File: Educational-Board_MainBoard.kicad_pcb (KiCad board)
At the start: 2 copper layers, 200 x 75.1 mm, 173 parts, among them J201 Screw_Terminal_01x02_P5mm, J202 USB-C_304A-ACP16X, J401 ACC_INT1, J402 BME_SPI, J403 LUX_INT, J501 RGB_OUT, J601 PWR_IN1, J602 PWR_IN2, J603 PWR_IN3, J604 PWR_IN4, J605 MCP_INT, J606 5V, J607 GND, J608 3V3, J609 EX_PA, J610 EX_PB, J611 PWR_OUT1, J612 PWR_OUT3, J613 PWR_OUT2, J614 PWR_OUT4, Q501 AO3400A, Q601 IRLML9301TRPBF, Q602 IRLML9301TRPBF, Q603 IRLML9301TRPBF, Q604 IRLML9301TRPBF, SW301 RESET, SW501 BUTTON1, SW502 BUTTON2, SW503 BUTTON3, SW504 BUTTON4, SW505 BUTTON5, U201 TPS5430DDA, U202 NUCLEO64-H503RB, U401 LSM6DS3, U402 BME280, U403 OPT4001, U404 INA2180A2, U406 YK16S-L7.2-B10Ka(32-8)-G-A29, U501 74LVC1G34, U502 SSD1315 OLED 0.98", U603 MCP23017_SS

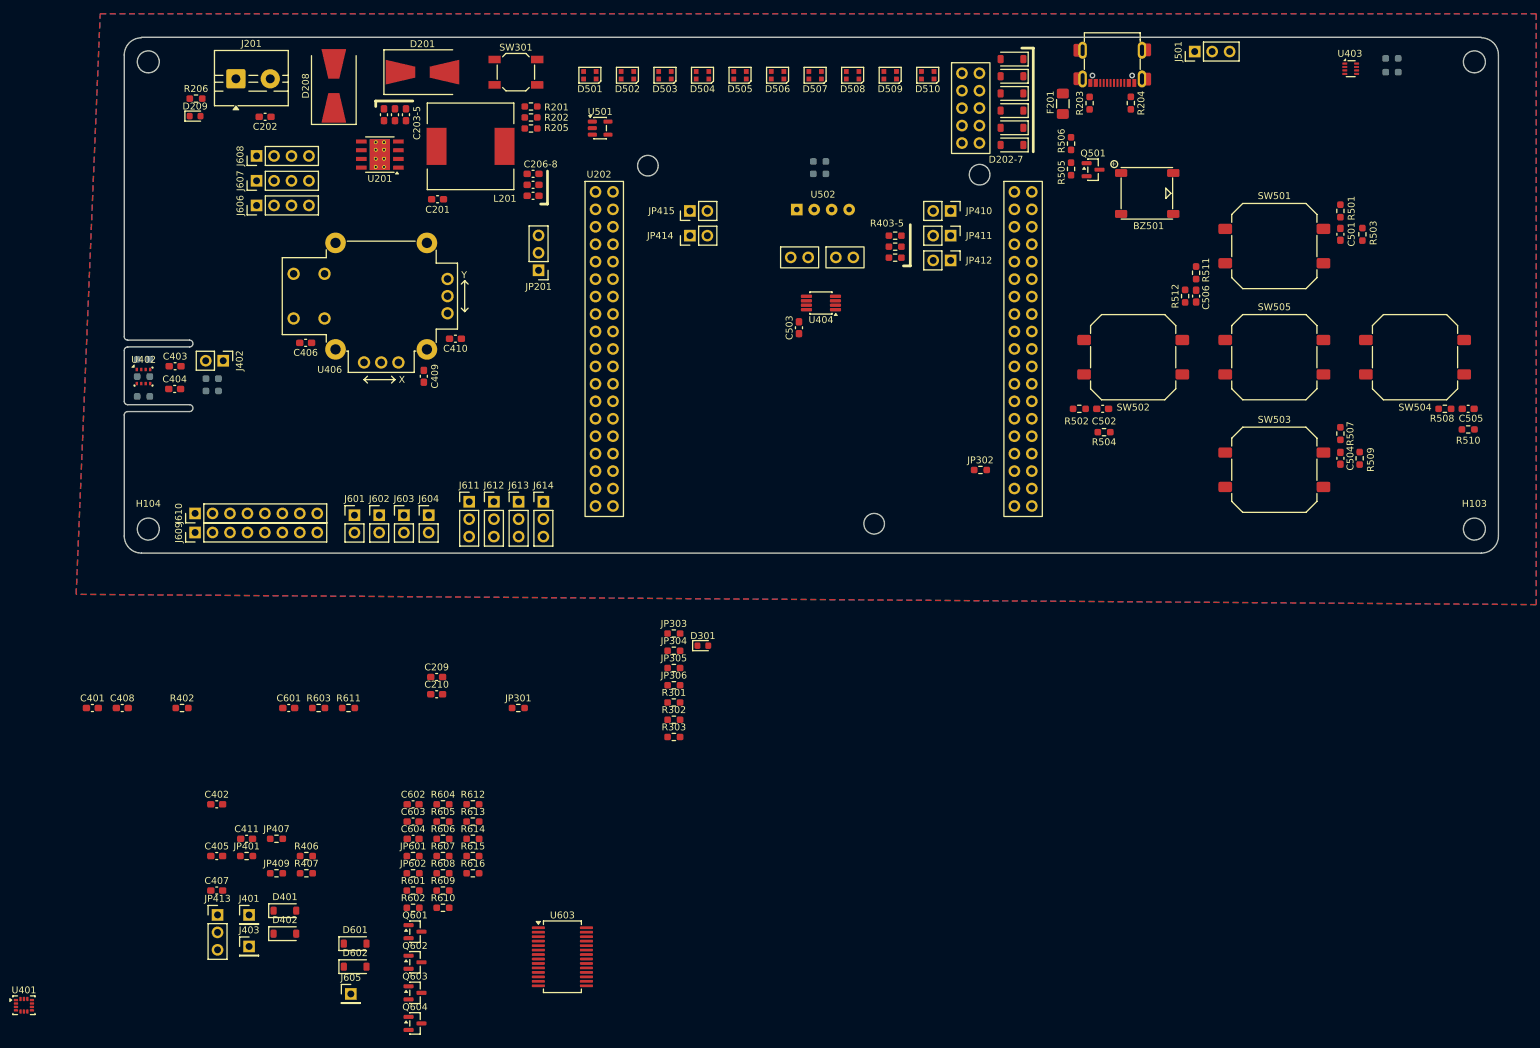
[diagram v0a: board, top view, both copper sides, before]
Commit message: Continued the floor plan
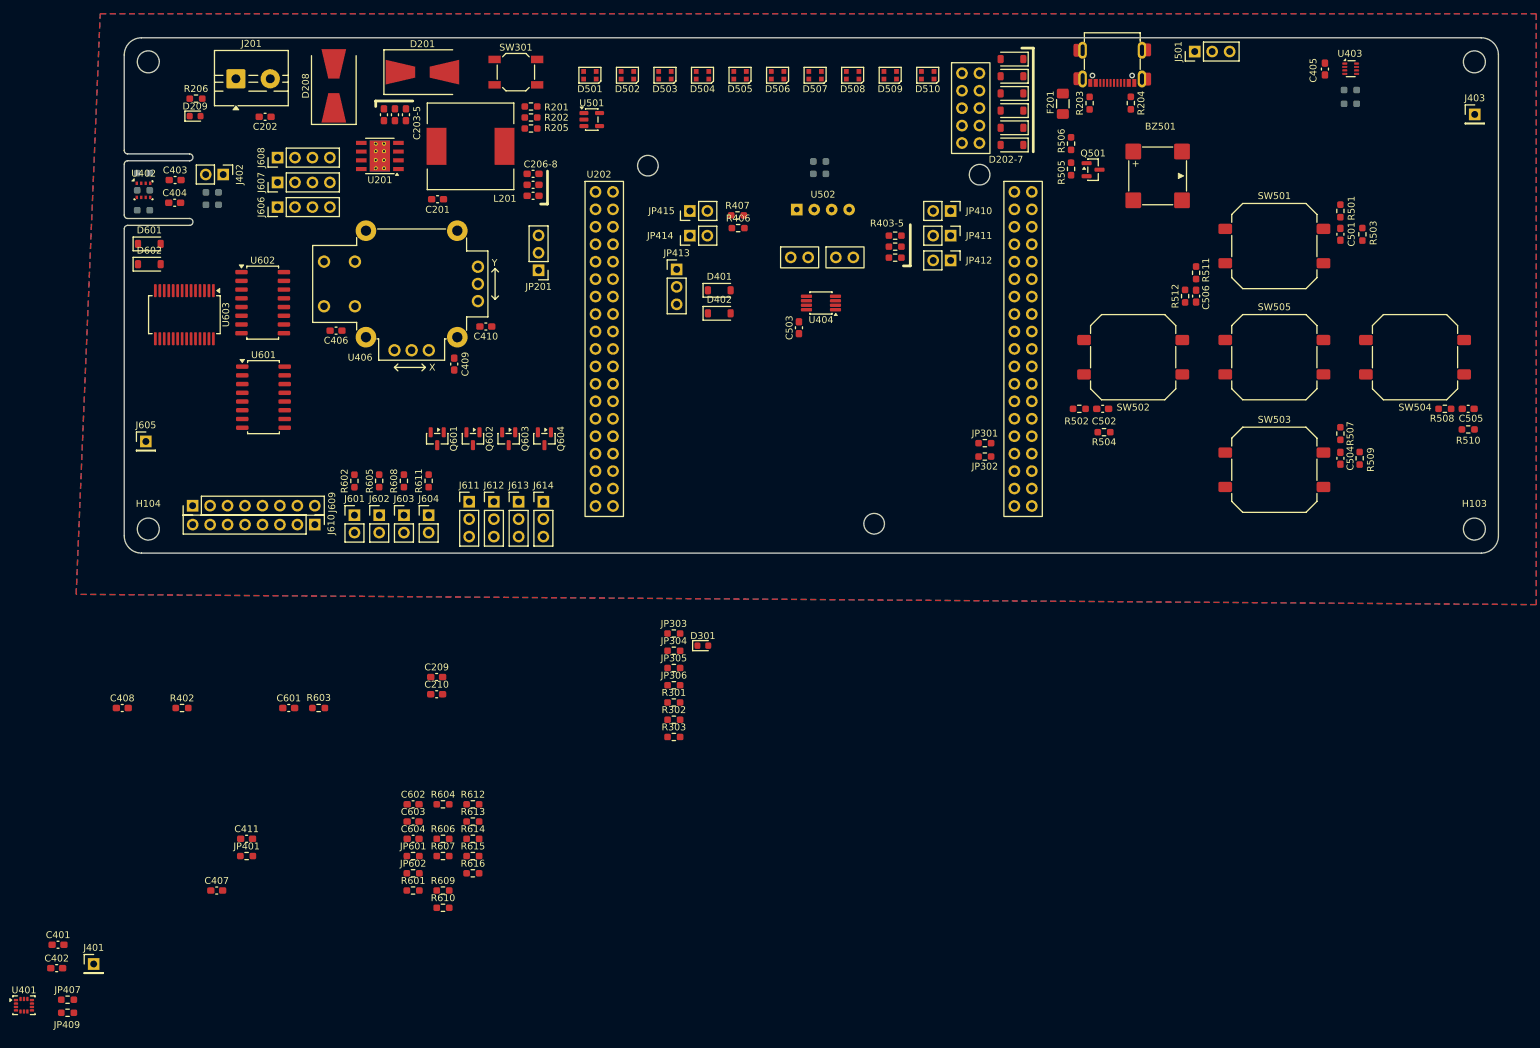
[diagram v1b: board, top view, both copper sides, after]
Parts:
- added U601: TLP291-4, Package_SO:SOP-16_4.4x10.4mm_P1.27mm, F.Cu at (70.3, 102.3)
- added U602: TLP291-4, Package_SO:SOP-16_4.4x10.4mm_P1.27mm, F.Cu at (70.2, 88.5)
- BZ501: footprint ProjectConnectors:Buzzer MLT-7525 -> ProjectConnectors:MLT-8530
- moved J403 215.6 mm to (246.6, 61.1)
- moved C405 197.8 mm to (224.8, 54.5), turned to -90 degrees
- moved JP413 115.3 mm to (130.4, 83.7)
- moved R407 114.5 mm to (139.2, 75.8)
- moved R406 110.9 mm to (139.3, 77.7)
- moved D401 110.2 mm to (136.6, 86.8)
- moved D402 110.2 mm to (136.6, 90.1)
- moved U603 108.4 mm to (58.8, 90.3), turned to -90 degrees
- moved D602 106.5 mm to (53.6, 83.0)
- moved D601 106.2 mm to (53.6, 80.0)
- moved Q604 87.2 mm to (111.2, 108.3), turned to -90 degrees
- moved J605 85.8 mm to (53.1, 108.8)
- moved Q603 81.8 mm to (106.0, 108.3), turned to -90 degrees
- moved JP301 78.1 mm to (175.2, 109.0)
- moved Q602 76.7 mm to (100.8, 108.3), turned to -90 degrees
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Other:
- board size 200 x 75.1 mm -> 200 x 75 mm

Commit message: some placement
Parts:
- D201, D208: value B560C -> B340A-13-F; footprint Diode_SMD:D_SMB-SMC_Universal_Handsoldering -> Diode_SMD:D_SMA
- L201: value 15uH 4.5A 32mOhm -> SLO0630H150MTT; footprint Inductor_SMD:L_12x12mm_H8mm -> Inductor_SMD:L_AVX_LMLP07A7
- R202: value 4K7 -> 4K3
- moved C210 107.8 mm to (161.5, 60.3)
- moved C209 107.1 mm to (161.5, 58.7)
- moved R206 88.2 mm to (148.6, 55.0), turned to 90 degrees
- moved D209 86.9 mm to (147.0, 55.1), turned to -90 degrees
- moved J201 63.8 mm to (130.0, 54.4), turned to 180 degrees
- moved D501 61.7 mm to (125.7, 116.6)
- moved D502 61.7 mm to (131.2, 116.6)
- moved D503 61.7 mm to (136.6, 116.6)
- moved D504 61.7 mm to (142.1, 116.6)
- moved D508 61.7 mm to (164.0, 116.6)
- moved D509 61.7 mm to (169.4, 116.6)
- moved D505 61.7 mm to (147.6, 116.6)
- moved D506 61.7 mm to (153.0, 116.6)
- moved D507 61.7 mm to (158.5, 116.6)
- moved D510 61.7 mm to (174.9, 116.6)
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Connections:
- J202 pad 5: /Power/D- -> unconnected-(J202-DN2-Pad5)
- J202 pad 6: /Power/D+ -> unconnected-(J202-DP1-Pad6)
- J202 pad 7: /Power/D- -> unconnected-(J202-DN1-Pad7)
- J202 pad 8: /Power/D+ -> unconnected-(J202-DP2-Pad8)

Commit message: Changed a bit the design, nothing important to note
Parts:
- moved J606 29.2 mm to (101.2, 70.7)
- moved J607 29.2 mm to (101.2, 67.1)
- moved J608 29.2 mm to (101.2, 63.5)
- moved SW301 3.77 mm to (109.8, 57.5)
- moved JP201 3.19 mm to (113.2, 82.6)
- moved D202 1.96 mm to (178.9, 66.3)
- moved D203 1.96 mm to (178.9, 63.8)
- moved D204 1.96 mm to (178.9, 61.3)
- moved D205 1.96 mm to (178.9, 58.8)
- moved D206 1.96 mm to (178.9, 56.3)
- moved D207 1.96 mm to (178.9, 53.8)

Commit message: Added some netclasses + started routing of some small parts + reordered some groups
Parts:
- added kibuzzard-69F1C39D: G***, kibuzzard-69F1C39D, F.Cu at (191.5, 65.9)
- added kibuzzard-69F1C39D: G***, kibuzzard-69F1C39D, F.Cu at (198.6, 58.4)
- added kibuzzard-69F1C3A3: G***, kibuzzard-69F1C3A3, F.Cu at (194.3, 65.9)
- added kibuzzard-69F1C3AE: G***, kibuzzard-69F1C3AE, F.Cu at (188.7, 65.9)
- added kibuzzard-69F1CCD6: G***, kibuzzard-69F1CCD6, F.Cu at (201.1, 58.4)
- added kibuzzard-69F1CD88: G***, kibuzzard-69F1CD88, F.Cu at (203.7, 58.3)
- JP402, JP403, JP404, JP405, JP406, JP408, JP501, JP502, R401: moved to F.Cu
- moved U401 219.2 mm to (217.8, 69.3)
- moved JP409 217.4 mm to (217.9, 64.5), turned to 180 degrees
- moved JP407 215.2 mm to (217.9, 66.3), turned to 180 degrees
- moved C402 209.6 mm to (216.9, 72.8), turned to -90 degrees
- moved C401 209.3 mm to (218.9, 72.8), turned to -90 degrees
- moved J401 204.0 mm to (213.7, 69.2)
- moved JP401 166.2 mm to (201.4, 70.3), turned to 180 degrees
- moved R402 163.3 mm to (201.4, 68.7), turned to 180 degrees
- moved J614 137.3 mm to (-26.2, 120.9), turned to -90 degrees
- moved J613 133.6 mm to (-26.2, 117.3), turned to -90 degrees
- moved J612 130.1 mm to (-26.2, 113.7), turned to -90 degrees
- moved Q604 128.8 mm to (-17.1, 121.0), turned to 180 degrees
- moved J611 126.6 mm to (-26.2, 110.1), turned to -90 degrees
- moved J604 123.4 mm to (-28.2, 104.2), turned to -90 degrees
- moved Q603 123.2 mm to (-17.1, 115.8), turned to 180 degrees
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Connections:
- JP405 pad 2: /POWER_UI/I2C_SCL -> /MCU/I2C_SCL
- JP406 pad 2: /POWER_UI/I2C_SCL -> /MCU/I2C_SCL
- JP409 pad 2: /POWER_UI/I2C_SCL -> /MCU/I2C_SCL
- JP502 pad 1: /POWER_UI/I2C_SCL -> /MCU/I2C_SCL
- JP602 pad 1: /POWER_UI/I2C_SCL -> /MCU/I2C_SCL
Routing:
- net +3V3: track 0.00 -> 45.0 mm
- net /Power/VUSB_FUSED: track 0.00 -> 31.0 mm
- net GND: track 0.00 -> 28.7 mm, vias 0 -> 3
- net Net-(J402-Pin_1): track 0.00 -> 16.3 mm
- net Net-(J402-Pin_2): track 0.00 -> 15.6 mm
- net Net-(JP406-A): track 0.00 -> 9.62 mm
- net Net-(JP408-A): track 0.00 -> 8.35 mm
- net /Power/VUSB: track 0.00 -> 7.86 mm
- net Net-(J202-CC2): track 0.00 -> 7.45 mm, vias 0 -> 2
- net Net-(J202-CC1): track 0.00 -> 7.25 mm, vias 0 -> 2
- net Net-(JP405-A): track 0.00 -> 7.02 mm
- net Net-(JP409-A): track 0.00 -> 6.17 mm
- net Net-(JP401-A): track 0.00 -> 5.15 mm
- net Net-(D205-A): track 0.00 -> 5.13 mm
- net Net-(D204-A): track 0.00 -> 5.09 mm
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- added copper zone on F.Cu, net +5V
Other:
- outline, holes or cut-outs redrawn

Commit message: Finished the netclass assignment
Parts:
- moved J601 23.0 mm to (-11.7, 77.4)
- moved J602 23.0 mm to (-11.7, 81.0)
- moved J603 23.0 mm to (-11.7, 84.6)
- moved J604 23.0 mm to (-11.7, 88.2)
- moved J609 23.0 mm to (-10.3, 53.9)
- moved J610 23.0 mm to (-13.1, 71.6)
- moved J611 23.0 mm to (-9.72, 94.1)
- moved J612 23.0 mm to (-9.72, 97.7)
- moved J613 23.0 mm to (-9.72, 101.3)
- moved J614 23.0 mm to (-9.72, 104.9)
- moved Q601 23.0 mm to (-0.55, 89.5)
- moved Q602 23.0 mm to (-0.55, 94.7)
- moved Q603 23.0 mm to (-0.55, 99.8)
- moved Q604 23.0 mm to (-0.55, 105.0)
- moved R602 23.0 mm to (-6.70, 77.4)
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
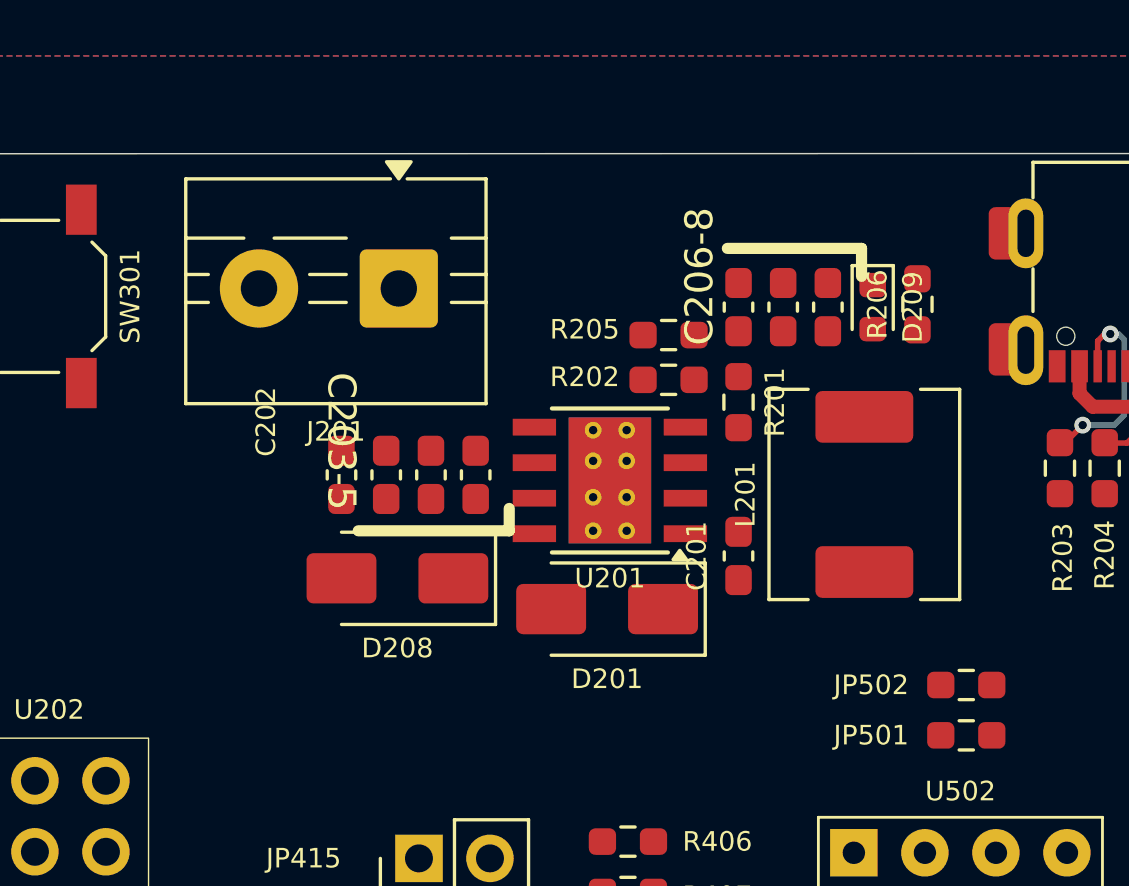
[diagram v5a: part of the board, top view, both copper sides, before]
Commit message: Routed the buck stage
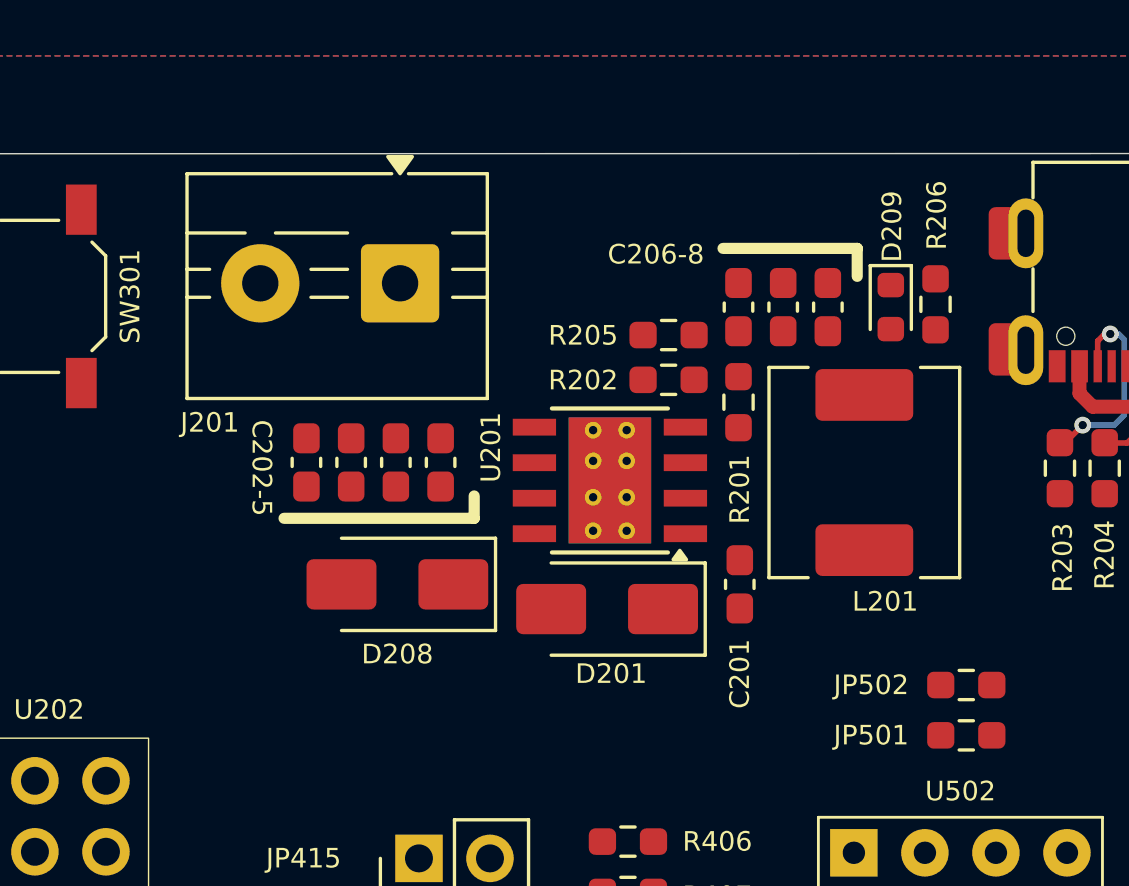
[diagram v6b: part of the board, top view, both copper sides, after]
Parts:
- moved C205 1.33 mm to (133.1, 61.0)
- moved C202 1.33 mm to (128.3, 61.0)
- moved C203 1.33 mm to (129.9, 61.0)
- moved C204 1.33 mm to (131.5, 61.0)
- moved C201 1.02 mm to (143.8, 65.4)
- moved L201 0.78 mm to (148.3, 61.4)
- moved R206 0.65 mm to (150.8, 55.4)
- moved D209 0.65 mm to (149.2, 55.5)
- moved D208 0.22 mm to (131.6, 65.4)
- moved J201 0.19 mm to (131.7, 54.6)
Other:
- board text added: "C202-5"
- board text removed: "C203-5"

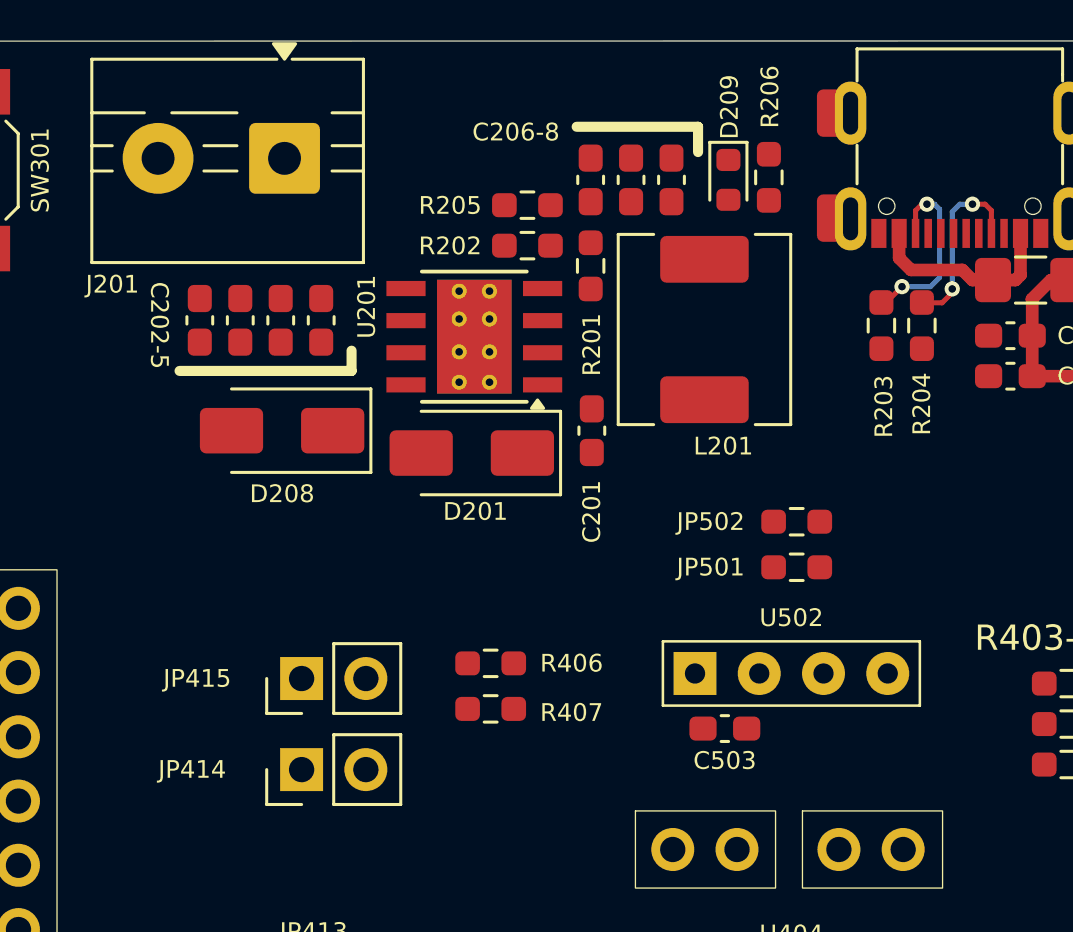
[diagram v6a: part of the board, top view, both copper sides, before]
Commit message: Updated the SSD1316 footprint
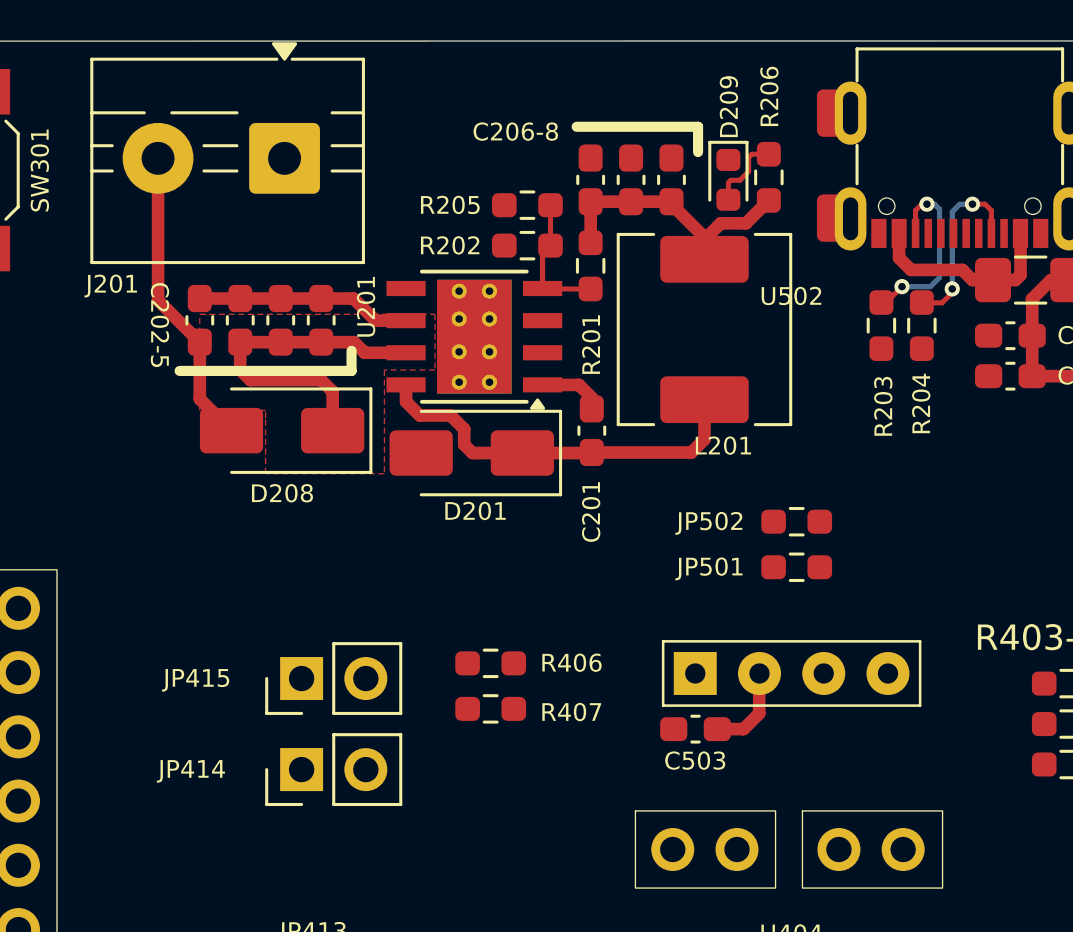
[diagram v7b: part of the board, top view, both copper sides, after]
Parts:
- moved U502 12.7 mm to (151.7, 75.0)
- moved C503 1.16 mm to (147.9, 77.2)
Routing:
- net /Power/PH_BUCK: track 0.00 -> 15.5 mm
- net VCC: track 0.00 -> 13.4 mm
- net /Power/VIN: track 0.00 -> 12.0 mm
- net /Power/OUT_BUCK: track 0.00 -> 11.6 mm
- net GND: track 28.7 -> 37.2 mm
- net /Power/VSENSE_BUCK: track 0.00 -> 5.33 mm
- net +3V3: track 45.0 -> 48.5 mm
- net Net-(D209-A): track 0.00 -> 3.06 mm
- net /Power/BOOT_BUCK: track 0.00 -> 2.60 mm
- added copper zone on F.Cu, net VCC
